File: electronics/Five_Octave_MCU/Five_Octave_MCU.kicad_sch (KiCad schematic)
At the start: 33 parts, among them J1 FFC Connector, J1 HRO_TYPE-C-31-M-12, SW21 Alps_Alpine_SKRP, SW22 Alps_Alpine_SKRP, U1 AP2112K-3.3, U2 Raspberry_Pi_RP2040, U3 W25Q64JVXGIQ, Y1 12MHz

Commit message: WIP
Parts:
- J1: LCSC (none) -> C165948
- LED1: LCSC (none) -> C2976072
- SW21, SW22: LCSC (none) -> C470426
- U1: LCSC (none) -> C51118
- U2: LCSC (none) -> C2040
- U2: renamed from U3; LCSC (none) -> C2940195
- Y1: LCSC (none) -> C9002
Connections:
- net COL0: now also U2.34 (GPIO22)
- net COL1: now also U2.35 (GPIO23)
- net COL2: now also U2.36 (GPIO24)
- net COL3: now also U2.37 (GPIO25)
- net COL4: now also U2.38 (GPIO26/ADC0)
- net COL5: now also U2.39 (GPIO27/ADC1)
- net COL6: now also U2.40 (GPIO28/ADC2)
- net COL7: now also U2.41 (GPIO29/ADC3)
- net ROW2: now also U2.27 (GPIO16)
- net ROW3: now also U2.28 (GPIO17)
- net ROW4: now also U2.29 (GPIO18)
- net ROW5: now also U2.30 (GPIO19)
- net ROW6: now also U2.31 (GPIO20)
- net ROW7: now also U2.32 (GPIO21)

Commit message: WIP
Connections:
- net ROW0: now also U2.17 (GPIO14)
- net ROW1: now also U2.18 (GPIO15)
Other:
- title: (none) -> Five Octave - MCU
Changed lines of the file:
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@@
 (kicad_sch (version 20230121) (generator eeschema)
   (paper "A4")
+  (title_block
+    (title "Five Octave - MCU")
+    (date "2023-08-14")
+    (rev "0.1.0-wip.1")
+    (comment 1 "https://github.com/takayoshiotake/five-octave-61-key-keyboard")
+  )
   (junction (at 133.985 57.785) (diameter 0) (color 0 0 0 0)
   )
@@
     )
   )
+  (global_label "ROW0" (shape input) (at 161.925 106.045 0) (fields_autoplaced)
+    (effects (font (size 1.27 1.27)) (justify left))
+    (property "Intersheetrefs" "${INTERSHEET_REFS}" (at 170.1716 106.045 0)
+      (effects (font (size 1.27 1.27)) (justify left) hide)
+    )
+  )
+  (global_label "ROW1" (shape input) (at 161.925 108.585 0) (fields_autoplaced)
+    (effects (font (size 1.27 1.27)) (justify left))
+    (property "Intersheetrefs" "${INTERSHEET_REFS}" (at 170.1716 108.585 0)
+      (effects (font (size 1.27 1.27)) (justify left) hide)
+    )
+  )

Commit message: Assign LCSC values
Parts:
- C1, C2: LCSC (none) -> C15525
- C10, C11, C12, C13, C14, C5, C6, C7, C8, C9: LCSC (none) -> C307331
- C15, C16: LCSC (none) -> C1570
- C3, C4: LCSC (none) -> C52923
- R1, R2: LCSC (none) -> C25905
- R3, R4: LCSC (none) -> C352446
- R5, R6: LCSC (none) -> C25744
- R7, R8: LCSC (none) -> C11702
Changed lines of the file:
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@@
     (title "Five Octave - MCU")
     (date "2023-08-14")
-    (rev "0.1.0-wip.1")
+    (rev "1.0.0-wip.1")
     (comment 1 "https://github.com/takayoshiotake/five-octave-61-key-keyboard")
   )
@@
       (effects (font (size 1.27 1.27)) hide)
     )
+    (property "LCSC" "C25744" (at 50.165 116.205 0)
+      (effects (font (size 1.27 1.27)) hide)
+    )
     (pin "1")
     (pin "2")
@@
       (effects (font (size 1.27 1.27)) hide)
     )
+    (property "LCSC" "C25905" (at 57.785 57.785 0)
+      (effects (font (size 1.27 1.27)) hide)
+    )
     (pin "1")
     (pin "2")
@@
       (effects (font (size 1.27 1.27)) hide)
     )
+    (property "LCSC" "C11702" (at 90.805 100.965 0)
+      (effects (font (size 1.27 1.27)) hide)
+    )
     (pin "1")
     (pin "2")
@@
       (effects (font (size 1.27 1.27)) hide)
     )
+    (property "LCSC" "C1570" (at 73.025 100.965 0)
+      (effects (font (size 1.27 1.27)) hide)
+    )
     (pin "1")
     (pin "2")
@@
     )
     (property "Datasheet" "~" (at 22.225 90.17 0)
+      (effects (font (size 1.27 1.27)) hide)
+    )
+    (property "LCSC" "C15525" (at 22.225 90.17 0)
       (effects (font (size 1.27 1.27)) hide)
     )
@@
       (effects (font (size 1.27 1.27)) hide)
     )
+    (property "LCSC" "C11702" (at 45.085 121.285 0)
+      (effects (font (size 1.27 1.27)) hide)
+    )
     (pin "1")
     (pin "2")
@@
       (effects (font (size 1.27 1.27)) hide)
     )
+    (property "LCSC" "C307331" (at 136.525 45.085 0)
+      (effects (font (size 1.27 1.27)) hide)
+    )
     (pin "1")
     (pin "2")
@@
       (effects (font (size 1.27 1.27)) hide)
     )
+    (property "LCSC" "C307331" (at 95.885 45.085 0)
+      (effects (font (size 1.27 1.27)) hide)
+    )
     (pin "1")
     (pin "2")
@@
     )
     (property "Datasheet" "~" (at 57.785 37.465 0)
+      (effects (font (size 1.27 1.27)) hide)
+    )
+    (property "LCSC" "C352446" (at 57.785 37.465 0)
       (effects (font (size 1.27 1.27)) hide)
     )
@@
       (effects (font (size 1.27 1.27)) hide)
     )
+    (property "LCSC" "C25744" (at 88.265 73.025 0)
+      (effects (font (size 1.27 1.27)) hide)
+    )
     (pin "1")
     (pin "2")
@@
       (effects (font (size 1.27 1.27)) hide)
     )
+    (property "LCSC" "C352446" (at 52.705 32.385 0)
+      (effects (font (size 1.27 1.27)) hide)
+    )
     (pin "1")
     (pin "2")
@@
       (effects (font (size 1.27 1.27)) hide)
     )
+    (property "LCSC" "C307331" (at 100.965 45.085 0)
+      (effects (font (size 1.27 1.27)) hide)
+    )
     (pin "1")
     (pin "2")
@@
     )
     (property "Datasheet" "~" (at 156.845 45.085 0)
+      (effects (font (size 1.27 1.27)) hide)
+    )
+    (property "LCSC" "C307331" (at 156.845 45.085 0)
       (effects (font (size 1.27 1.27)) hide)
     )
@@
       (effects (font (size 1.27 1.27)) hide)
     )
+    (property "LCSC" "C307331" (at 141.605 45.085 0)
+      (effects (font (size 1.27 1.27)) hide)
+    )
     (pin "1")
     (pin "2")
@@
     )
     (property "Datasheet" "~" (at 161.925 45.085 0)
+      (effects (font (size 1.27 1.27)) hide)
+    )
+    (property "LCSC" "C307331" (at 161.925 45.085 0)
       (effects (font (size 1.27 1.27)) hide)
     )
@@
       (effects (font (size 1.27 1.27)) hide)
     )
+    (property "LCSC" "C307331" (at 167.005 45.085 0)
+      (effects (font (size 1.27 1.27)) hide)
+    )
     (pin "1")
     (pin "2")
@@
       (effects (font (size 1.27 1.27)) hide)
     )
+    (property "LCSC" "C52923" (at 111.125 45.085 0)
+      (effects (font (size 1.27 1.27)) hide)
+    )
     (pin "1")
     (pin "2")
@@
     )
     (property "Datasheet" "~" (at 126.365 45.085 0)
+      (effects (font (size 1.27 1.27)) hide)
+    )
+    (property "LCSC" "C52923" (at 126.365 45.085 0)
       (effects (font (size 1.27 1.27)) hide)
     )
@@
       (effects (font (size 1.27 1.27)) hide)
     )
+    (property "LCSC" "C307331" (at 146.685 45.085 0)
+      (effects (font (size 1.27 1.27)) hide)
+    )
     (pin "1")
     (pin "2")
@@
       (effects (font (size 1.27 1.27)) hide)
     )
+    (property "LCSC" "C307331" (at 172.085 45.085 0)
+      (effects (font (size 1.27 1.27)) hide)
+    )
     (pin "1")
     (pin "2")
@@
     )
     (property "Datasheet" "~" (at 52.705 52.705 0)
+      (effects (font (size 1.27 1.27)) hide)
+    )
+    (property "LCSC" "C25905" (at 52.705 52.705 0)
       (effects (font (size 1.27 1.27)) hide)
     )
@@
       (effects (font (size 1.27 1.27)) hide)
     )
+    (property "LCSC" "C15525" (at 50.165 90.17 0)
+      (effects (font (size 1.27 1.27)) hide)
+    )
     (pin "1")
     (pin "2")
@@
       (effects (font (size 1.27 1.27)) hide)
     )
+    (property "LCSC" "C1570" (at 73.025 93.345 0)
+      (effects (font (size 1.27 1.27)) hide)
+    )
     (pin "1")
     (pin "2")
@@
       (effects (font (size 1.27 1.27)) hide)
     )
+    (property "LCSC" "C307331" (at 151.765 45.085 0)
+      (effects (font (size 1.27 1.27)) hide)
+    )

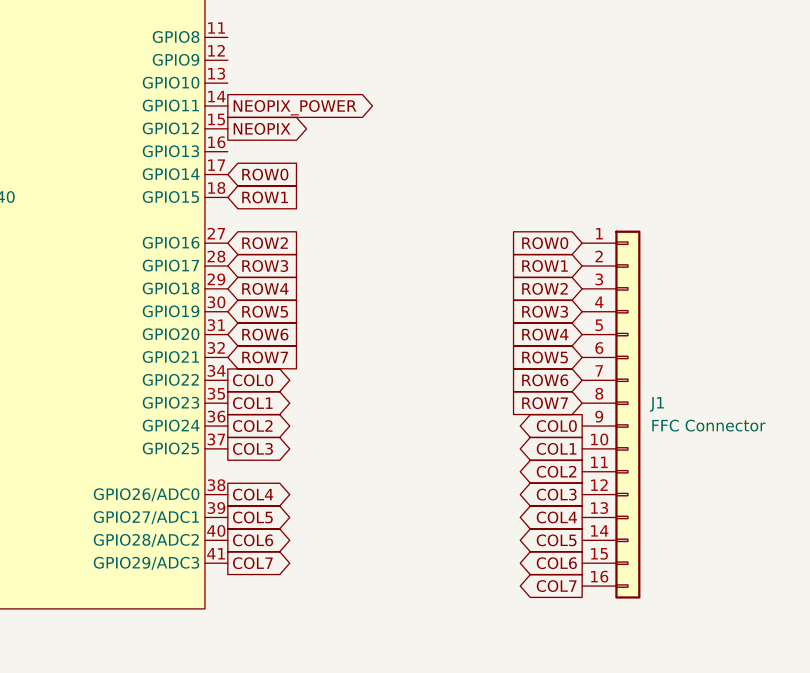
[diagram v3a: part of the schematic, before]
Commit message: Fix FFC connector assignment
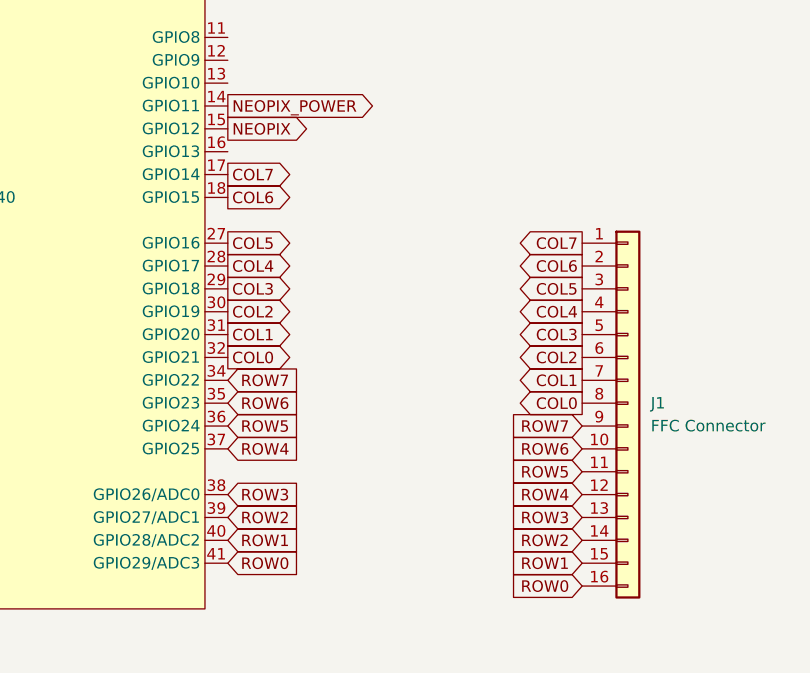
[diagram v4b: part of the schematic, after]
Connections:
- net COL0: now also J1.8 (Pin_8), U2.32 (GPIO21); no longer J1.9 (Pin_9), U2.34 (GPIO22)
- net COL1: now also J1.7 (Pin_7), U2.31 (GPIO20); no longer J1.10 (Pin_10), U2.35 (GPIO23)
- net COL2: now also J1.6 (Pin_6), U2.30 (GPIO19); no longer J1.11 (Pin_11), U2.36 (GPIO24)
- net COL3: now also J1.5 (Pin_5), U2.29 (GPIO18); no longer J1.12 (Pin_12), U2.37 (GPIO25)
- net COL4: now also J1.4 (Pin_4), U2.28 (GPIO17); no longer J1.13 (Pin_13), U2.38 (GPIO26/ADC0)
- net COL5: now also J1.3 (Pin_3), U2.27 (GPIO16); no longer J1.14 (Pin_14), U2.39 (GPIO27/ADC1)
- net COL6: now also J1.2 (Pin_2), U2.18 (GPIO15); no longer J1.15 (Pin_15), U2.40 (GPIO28/ADC2)
- net COL7: now also J1.1 (Pin_1), U2.17 (GPIO14); no longer J1.16 (Pin_16), U2.41 (GPIO29/ADC3)
- net ROW0: now also J1.16 (Pin_16), U2.41 (GPIO29/ADC3); no longer J1.1 (Pin_1), U2.17 (GPIO14)
- net ROW1: now also J1.15 (Pin_15), U2.40 (GPIO28/ADC2); no longer J1.2 (Pin_2), U2.18 (GPIO15)
- net ROW2: now also J1.14 (Pin_14), U2.39 (GPIO27/ADC1); no longer J1.3 (Pin_3), U2.27 (GPIO16)
- net ROW3: now also J1.13 (Pin_13), U2.38 (GPIO26/ADC0); no longer J1.4 (Pin_4), U2.28 (GPIO17)
- net ROW4: now also J1.12 (Pin_12), U2.37 (GPIO25); no longer J1.5 (Pin_5), U2.29 (GPIO18)
- net ROW5: now also J1.11 (Pin_11), U2.36 (GPIO24); no longer J1.6 (Pin_6), U2.30 (GPIO19)
- net ROW6: now also J1.10 (Pin_10), U2.35 (GPIO23); no longer J1.7 (Pin_7), U2.31 (GPIO20)
- net ROW7: now also J1.9 (Pin_9), U2.34 (GPIO22); no longer J1.8 (Pin_8), U2.32 (GPIO21)

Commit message: Change footprint for AP2112K-3.3
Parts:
- U1: footprint Package_TO_SOT_SMD:SOT-23-5 -> Project_Library:SOT-23-5
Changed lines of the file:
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@@
       (effects (font (size 1.27 1.27)))
     )
-    (property "Footprint" "Package_TO_SOT_SMD:SOT-23-5" (at 37.465 79.375 0)
+    (property "Footprint" "Project_Library:SOT-23-5" (at 37.465 79.375 0)
       (effects (font (size 1.27 1.27)) hide)
     )
